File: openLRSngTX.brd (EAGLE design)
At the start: 50 x 40 mm, 33 parts, among them IC1 RFM23BPSMD, J1 AVR_SPI_PRG_6PTH, Q1 MMBT2222, U1 ATMEGA328P, X1 BU-SMA-V, Y1 16MHz

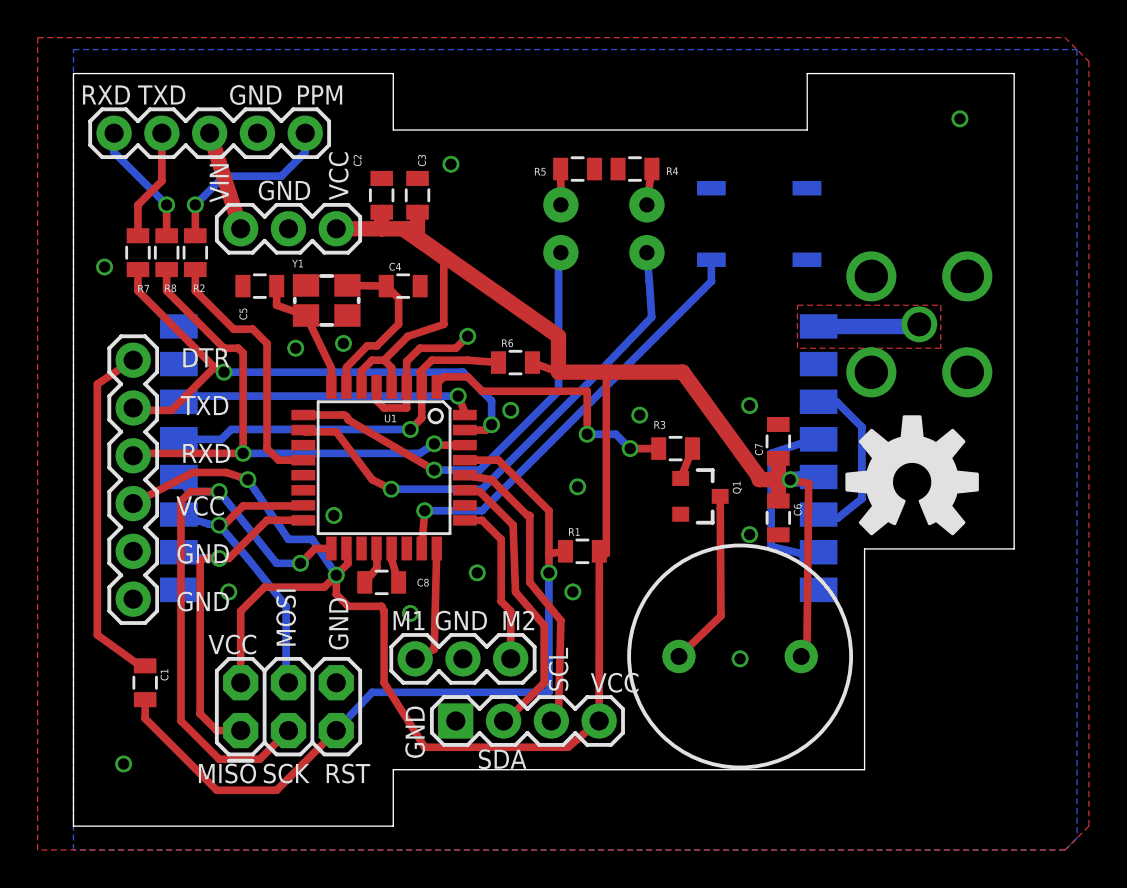
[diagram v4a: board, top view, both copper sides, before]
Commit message: Add possibility for wired boind button.
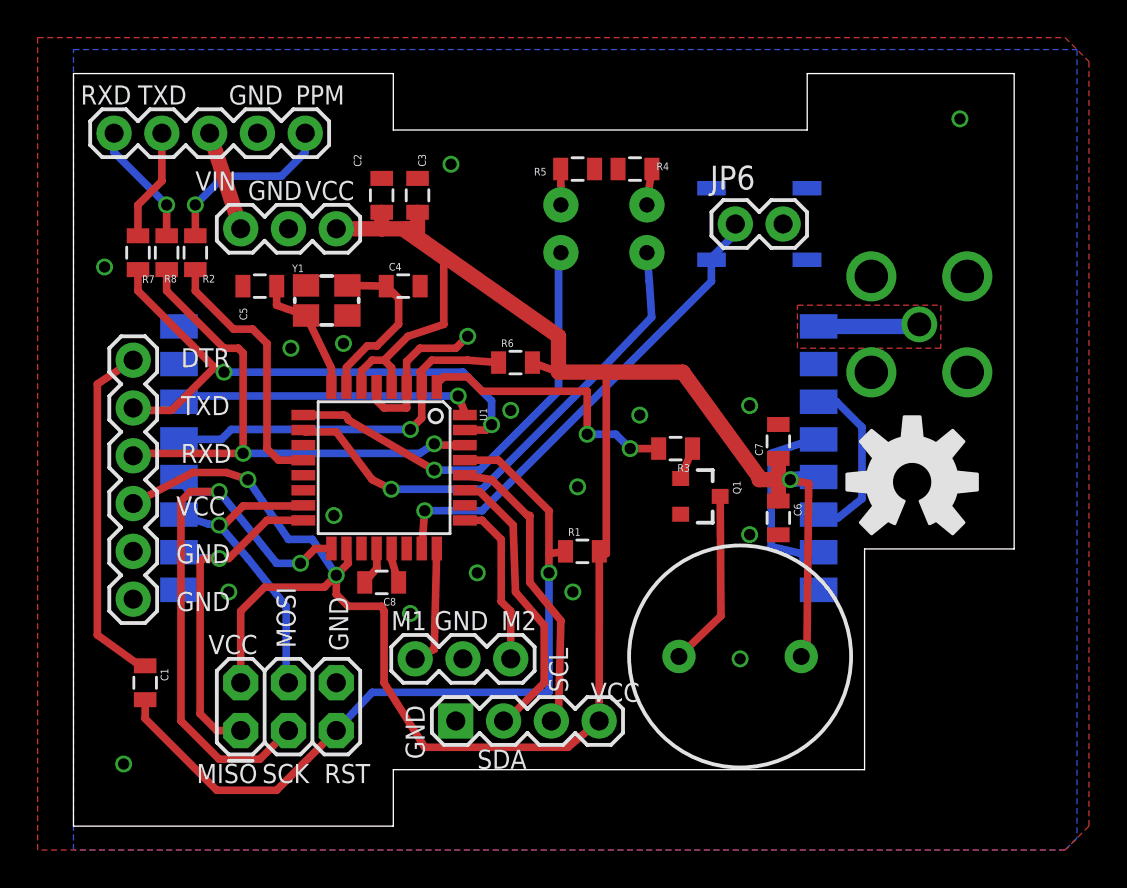
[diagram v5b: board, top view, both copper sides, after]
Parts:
- added JP6: (no value), SparkFun-Connectors:1X02
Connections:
- net GND: now also JP6.2
- net N$15: now also JP6.1
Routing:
- net N$15: track 23.4 -> 25.9 mm
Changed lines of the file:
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@@
 <layer number="27" name="tValues" color="7" fill="1" visible="yes" active="yes"/>
 <layer number="28" name="bValues" color="7" fill="1" visible="yes" active="yes"/>
-<layer number="29" name="tStop" color="7" fill="3" visible="yes" active="yes"/>
+<layer number="29" name="tStop" color="7" fill="3" visible="no" active="yes"/>
 <layer number="30" name="bStop" color="7" fill="6" visible="no" active="yes"/>
 <layer number="31" name="tCream" color="7" fill="4" visible="no" active="yes"/>
@@
 <text x="11.176" y="38.354" size="1.016" layer="25">PPM</text>
 <text x="7.62" y="38.354" size="1.016" layer="25">GND</text>
-<text x="6.604" y="35.306" size="1.016" layer="25" rot="R270">VIN</text>
+<text x="5.842" y="33.782" size="1.016" layer="25">VIN</text>
 <text x="2.794" y="38.354" size="1.016" layer="25">TXD</text>
-<text x="13.97" y="33.274" size="1.016" layer="25" rot="R90">VCC</text>
-<text x="9.144" y="33.274" size="1.016" layer="25">GND</text>
+<text x="11.684" y="33.274" size="1.016" layer="25">VCC</text>
+<text x="8.636" y="33.274" size="1.016" layer="25">GND</text>
 <text x="18.034" y="3.556" size="1.016" layer="25" rot="R90">GND</text>
 <text x="20.828" y="3.048" size="1.016" layer="25">SDA</text>
 <text x="25.654" y="7.112" size="1.016" layer="25" rot="R90">SCL</text>
-<text x="29.464" y="8.128" size="1.016" layer="25" rot="R180">VCC</text>
+<text x="29.464" y="7.62" size="1.016" layer="25" rot="R180">VCC</text>
 <text x="9.144" y="10.16" size="1.016" layer="25" rot="R180">VCC</text>
 <text x="9.144" y="3.302" size="1.016" layer="25" rot="R180">MISO</text>
@@
 </autorouter>
 <elements>
-<element name="U1" library="SparkFun-DigitalIC" package="TQFP32-08" value="ATMEGA328P" x="15.875" y="19.05" smashed="yes" rot="R270">
+<element name="U1" library="SparkFun-DigitalIC" package="TQFP32-08" value="ATMEGA328P" x="15.875" y="19.05" rot="R270">
 <attribute name="PROD_ID" value="IC-09069" x="-8.255" y="1.27" size="1.778" layer="27" rot="R270" display="off"/>
-<attribute name="NAME" x="15.875" y="21.463" size="0.4064" layer="25"/>
-<attribute name="VALUE" x="9.525" y="21.59" size="0.4064" layer="27" rot="R270"/>
 </element>
 <element name="C1" library="SparkFun-Capacitors" package="0805" value="100n" x="3.175" y="7.62" rot="R270"/>
@@
 <element name="R1" library="SparkFun-Resistors" package="0805" value="10k" x="26.416" y="14.605"/>
 <element name="R2" library="SparkFun-Resistors" package="0805" value="1k" x="5.842" y="30.48" smashed="yes" rot="R270">
-<attribute name="NAME" x="5.715" y="28.3845" size="0.4064" layer="25"/>
-<attribute name="VALUE" x="5.7785" y="27.813" size="0.4064" layer="27"/>
-</element>
-<element name="R3" library="SparkFun-Resistors" package="0805" value="1k" x="31.369" y="20.066" smashed="yes" rot="R180">
-<attribute name="NAME" x="30.861" y="21.5265" size="0.4064" layer="25" rot="R180"/>
-<attribute name="VALUE" x="31.877" y="21.463" size="0.4064" layer="27" rot="R180"/>
-</element>
+<attribute name="NAME" x="6.223" y="28.8925" size="0.4064" layer="25"/>
+<attribute name="VALUE" x="6.2865" y="28.321" size="0.4064" layer="27"/>
+</element>
+<element name="R3" library="SparkFun-Resistors" package="0805" value="1k" x="31.369" y="20.066" rot="R180"/>
 <element name="R4" library="SparkFun-Resistors" package="0805" value="220R" x="29.21" y="34.925" smashed="yes">
-<attribute name="NAME" x="30.861" y="34.6075" size="0.4064" layer="25"/>
-<attribute name="VALUE" x="28.6385" y="35.814" size="0.4064" layer="27"/>
+<attribute name="NAME" x="30.353" y="34.8615" size="0.4064" layer="25"/>
+<attribute name="VALUE" x="28.6385" y="35.56" size="0.4064" layer="27"/>
 </element>
 <element name="R5" library="SparkFun-Resistors" package="0805" value="220R" x="26.162" y="34.925" smashed="yes" rot="R180">
 <attribute name="NAME" x="24.511" y="34.9885" size="0.4064" layer="25" rot="R180"/>
-<attribute name="VALUE" x="26.4795" y="36.322" size="0.4064" layer="27" rot="R180"/>
+<attribute name="VALUE" x="26.4795" y="36.068" size="0.4064" layer="27" rot="R180"/>
 </element>
 <element name="LED1" library="SparkFun-LED" package="LED3MM" value="RED" x="29.845" y="31.75" smashed="yes" rot="MR90"/>
@@
 <attribute name="OC_FARNELL" value="unknown" x="44.323" y="26.67" size="1.778" layer="28" rot="MR0" display="off"/>
 </element>
-<element name="Y1" library="crystal_3225" package="CRYSTAL-SMD-5X3" value="16MHz" x="12.827" y="27.94" smashed="yes">
-<attribute name="NAME" x="10.987" y="29.699" size="0.4064" layer="25"/>
-<attribute name="VALUE" x="10.987" y="25.846" size="0.4064" layer="27"/>
-</element>
+<element name="Y1" library="crystal_3225" package="CRYSTAL-SMD-5X3" value="16MHz" x="12.827" y="27.94"/>
 <element name="JP1" library="SparkFun-Connectors" package="1X05" value="IN" x="11.684" y="36.83" smashed="yes" rot="R180"/>
 <element name="JP4" library="SparkFun-Connectors" package="1X03" value="REG" x="8.255" y="31.75" smashed="yes"/>
@@
 <element name="C7" library="SparkFun-Capacitors" package="0805" value="100n" x="36.83" y="20.447" rot="R90"/>
 <element name="R6" library="SparkFun-Resistors" package="0805" value="1k" x="22.86" y="24.638"/>
-<element name="C8" library="SparkFun-Capacitors" package="0805" value="100n" x="15.748" y="12.954" smashed="yes" rot="R180">
-<attribute name="NAME" x="18.288" y="13.1445" size="0.4064" layer="25" rot="R180"/>
-<attribute name="VALUE" x="18.796" y="13.843" size="0.4064" layer="27" rot="R180"/>
-</element>
+<element name="C8" library="SparkFun-Capacitors" package="0805" value="100n" x="15.748" y="12.954" rot="R180"/>
 <element name="S1" library="SparkFun-Electromechanical" package="TACTILE_SWITCH_SMD" value="SWITCH-MOMENTARY-2SMD" x="35.814" y="32.004" smashed="yes" rot="MR180">
 <attribute name="VALUE" x="34.925" y="34.036" size="0.4064" layer="28" rot="MR180"/>
 </element>
 <element name="R7" library="SparkFun-Resistors" package="0805" value="1k" x="2.794" y="30.48" smashed="yes" rot="R270">
-<attribute name="NAME" x="3.429" y="28.7655" size="0.4064" layer="25" rot="R180"/>
-<attribute name="VALUE" x="2.7305" y="27.813" size="0.4064" layer="27"/>
+<attribute name="NAME" x="3.683" y="29.2735" size="0.4064" layer="25" rot="R180"/>
+<attribute name="VALUE" x="2.9845" y="28.321" size="0.4064" layer="27"/>
 </element>
 <element name="U$1" library="SparkFun-Aesthetics" package="OSHW-LOGO-L" value="" x="43.942" y="18.288" rot="MR0"/>
@@
 <element name="U$2" library="SparkFun-Aesthetics" package="OSHW-LOGO-L" value="" x="43.942" y="18.288"/>
 <element name="R8" library="SparkFun-Resistors" package="0805" value="1k" x="4.318" y="30.48" smashed="yes" rot="R270">
-<attribute name="NAME" x="4.191" y="28.3845" size="0.4064" layer="25"/>
-<attribute name="VALUE" x="4.2545" y="27.813" size="0.4064" layer="27"/>
-</element>
+<attribute name="NAME" x="4.191" y="28.8925" size="0.4064" layer="25"/>
+<attribute name="VALUE" x="4.2545" y="28.321" size="0.4064" layer="27"/>
+</element>
+<element name="JP6" library="SparkFun-Connectors" package="1X02" value="" x="34.544" y="32.004"/>
 </elements>
 <signals>
@@
 <contactref element="Y1" pad="2"/>
 <via x="13.716" y="25.654" extent="1-16" drill="0.6"/>
-<via x="11.176" y="25.4" extent="1-16" drill="0.6"/>
+<via x="10.922" y="25.4" extent="1-16" drill="0.6"/>
 <via x="13.208" y="16.51" extent="1-16" drill="0.6"/>
+<contactref element="JP6" pad="2"/>
 </signal>
 <signal name="VCC">
@@
 <wire x1="33.274" y1="28.956" x2="33.274" y2="30.099" width="0.4064" layer="16"/>
 <wire x1="18.034" y1="16.764" x2="17.875" y2="14.7574" width="0.4064" layer="1"/>
+<contactref element="JP6" pad="1"/>
+<wire x1="33.274" y1="30.099" x2="33.274" y2="30.226" width="0.4064" layer="16"/>
+<wire x1="33.274" y1="30.226" x2="34.544" y2="31.496" width="0.4064" layer="16"/>
+<wire x1="34.544" y1="31.496" x2="34.544" y2="32.004" width="0.4064" layer="16"/>
 </signal>
 <signal name="N$16">

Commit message: Add mountting holes.
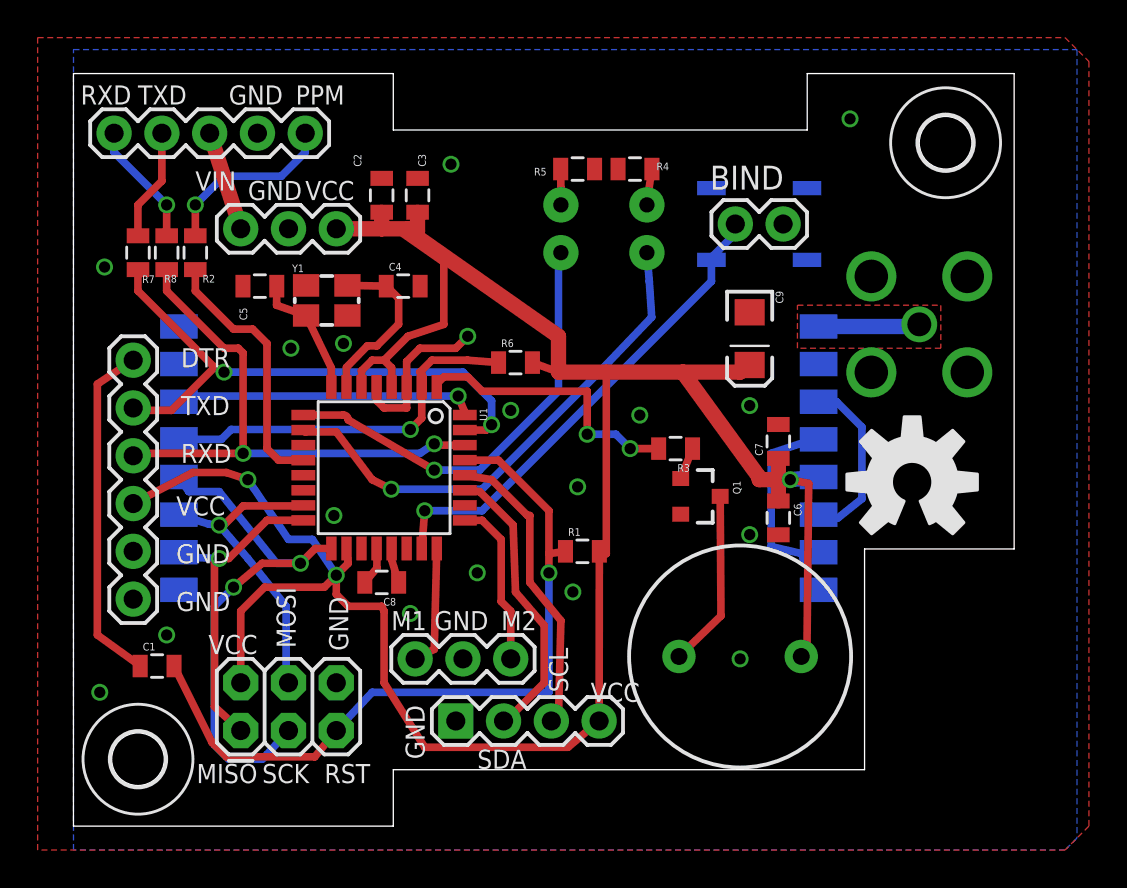
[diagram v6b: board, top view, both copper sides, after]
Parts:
- added C9: 10uF, SparkFun-Capacitors:EIA3216
- added U$3, U$4: (no value), holes:2,8
- S1: value SWITCH-MOMENTARY-2SMD -> BIND
- moved C1 1.09 mm to (3.81, 8.51), turned to 0 degrees
- renumbered JP6 to BIND
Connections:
- net GND: now also C9.C
- net VCC: now also C9.A
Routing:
- net VCC: track 129.4 -> 133.1 mm
- net SCK: track 31.8 -> 28.4 mm
- net /RESET: track 42.4 -> 40.4 mm
- net MISO: track 19.3 -> 17.5 mm
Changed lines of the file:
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@@
 <attribute name="PROD_ID" value="IC-09069" x="-8.255" y="1.27" size="1.778" layer="27" rot="R270" display="off"/>
 </element>
-<element name="C1" library="SparkFun-Capacitors" package="0805" value="100n" x="3.175" y="7.62" rot="R270"/>
+<element name="C1" library="SparkFun-Capacitors" package="0805" value="100n" x="3.81" y="8.509"/>
 <element name="C2" library="SparkFun-Capacitors" package="0805" value="100n" x="15.748" y="33.528" smashed="yes" rot="R90">
 <attribute name="NAME" x="14.6685" y="35.052" size="0.4064" layer="25" rot="R90"/>
@@
 <element name="R6" library="SparkFun-Resistors" package="0805" value="1k" x="22.86" y="24.638"/>
 <element name="C8" library="SparkFun-Capacitors" package="0805" value="100n" x="15.748" y="12.954" rot="R180"/>
-<element name="S1" library="SparkFun-Electromechanical" package="TACTILE_SWITCH_SMD" value="SWITCH-MOMENTARY-2SMD" x="35.814" y="32.004" smashed="yes" rot="MR180">
+<element name="S1" library="SparkFun-Electromechanical" package="TACTILE_SWITCH_SMD" value="BIND" x="35.814" y="32.004" smashed="yes" rot="MR180">
 <attribute name="VALUE" x="34.925" y="34.036" size="0.4064" layer="28" rot="MR180"/>
 </element>
@@
 <attribute name="VALUE" x="4.2545" y="28.321" size="0.4064" layer="27"/>
 </element>
-<element name="JP6" library="SparkFun-Connectors" package="1X02" value="" x="34.544" y="32.004"/>
+<element name="BIND" library="SparkFun-Connectors" package="1X02" value="" x="34.544" y="32.004"/>
+<element name="U$3" library="holes" package="2,8" value="" x="2.794" y="3.556"/>
+<element name="U$4" library="holes" package="2,8" value="" x="45.72" y="36.322"/>
+<element name="C9" library="SparkFun-Capacitors" package="EIA3216" value="10uF" x="35.306" y="25.908" rot="R270">
+<attribute name="PROD_ID" value="CAP-00811" x="35.306" y="25.908" size="1.778" layer="27" rot="R270" display="off"/>
+</element>
 </elements>
 <signals>
@@
 <contactref element="S1" pad="3"/>
 <via x="35.306" y="15.494" extent="1-16" drill="0.6"/>
-<via x="7.62" y="12.446" extent="1-16" drill="0.6"/>
+<via x="4.318" y="10.16" extent="1-16" drill="0.6"/>
 <via x="25.908" y="12.446" extent="1-16" drill="0.6"/>
 <via x="26.162" y="18.034" extent="1-16" drill="0.6"/>
@@
 <via x="29.464" y="21.844" extent="1-16" drill="0.6"/>
 <via x="20.828" y="13.462" extent="1-16" drill="0.6"/>
-<via x="2.032" y="3.302" extent="1-16" drill="0.6"/>
-<via x="46.482" y="37.592" extent="1-16" drill="0.6"/>
+<via x="0.762" y="7.112" extent="1-16" drill="0.6"/>
+<via x="40.64" y="37.592" extent="1-16" drill="0.6"/>
 <contactref element="JP5" pad="2"/>
 <wire x1="16.275" y1="14.7574" x2="16.256" y2="14.224" width="0.4064" layer="1"/>
@@
 <via x="10.922" y="25.4" extent="1-16" drill="0.6"/>
 <via x="13.208" y="16.51" extent="1-16" drill="0.6"/>
-<contactref element="JP6" pad="2"/>
+<contactref element="BIND" pad="2"/>
+<contactref element="C9" pad="C"/>
 </signal>
 <signal name="VCC">
@@
 <wire x1="38.443603125" y1="18.21205" x2="37.465" y2="18.415" width="0.4064" layer="1"/>
 <wire x1="27.686" y1="14.478" x2="27.316" y2="14.605" width="0.4064" layer="1"/>
+<contactref element="C9" pad="A"/>
+<wire x1="31.75" y1="24.13" x2="34.798" y2="24.13" width="0.8128" layer="1"/>
+<wire x1="34.798" y1="24.13" x2="35.306" y2="24.508" width="0.8128" layer="1"/>
 </signal>
 <signal name="RXD">
@@
 <wire x1="0.635" y1="23.495" x2="0.635" y2="10.16" width="0.4064" layer="1"/>
 <wire x1="0.635" y1="10.16" x2="2.91" y2="8.52" width="0.4064" layer="1"/>
-<wire x1="2.91" y1="8.52" x2="3.175" y2="8.52" width="0.4064" layer="1"/>
+<wire x1="2.91" y1="8.52" x2="2.91" y2="8.509" width="0.4064" layer="1"/>
 </signal>
 <signal name="/RESET">
@@
 <contactref element="U1" pad="29"/>
 <contactref element="J1" pad="5"/>
-<wire x1="3.175" y1="6.72" x2="3.175" y2="5.715" width="0.4064" layer="1"/>
-<wire x1="3.175" y1="5.715" x2="6.985" y2="1.905" width="0.4064" layer="1"/>
-<wire x1="6.985" y1="1.905" x2="10.16" y2="1.905" width="0.4064" layer="1"/>
-<wire x1="10.16" y1="1.905" x2="13.335" y2="5.08" width="0.4064" layer="1"/>
+<wire x1="4.71" y1="8.509" x2="6.731" y2="4.445" width="0.4064" layer="1"/>
+<wire x1="6.731" y1="4.445" x2="7.493" y2="3.683" width="0.4064" layer="1"/>
+<wire x1="7.493" y1="3.683" x2="12.192" y2="3.683" width="0.4064" layer="1"/>
+<wire x1="12.192" y1="3.683" x2="13.335" y2="5.08" width="0.4064" layer="1"/>
 <wire x1="20.1676" y1="19.45" x2="21.952" y2="19.45" width="0.4064" layer="1"/>
 <wire x1="21.952" y1="19.45" x2="24.638" y2="16.764" width="0.4064" layer="1"/>
@@
 <contactref element="U1" pad="16"/>
 <contactref element="IC1" pad="10"/>
-<wire x1="8.255" y1="5.08" x2="6.985" y2="5.08" width="0.4064" layer="1"/>
-<wire x1="6.985" y1="5.08" x2="6.096" y2="5.969" width="0.4064" layer="1"/>
 <wire x1="11.5824" y1="16.25" x2="11.5764" y2="16.256" width="0.4064" layer="1"/>
 <wire x1="11.5764" y1="16.256" x2="9.652" y2="16.256" width="0.4064" layer="1"/>
@@
 <wire x1="7.112" y1="14.224" x2="5.16" y2="14.304" width="0.4064" layer="16"/>
 <wire x1="5.16" y1="14.304" x2="4.971" y2="14.558" width="0.4064" layer="16"/>
-<wire x1="6.096" y1="5.969" x2="6.096" y2="14.05" width="0.4064" layer="1"/>
-<wire x1="6.096" y1="14.05" x2="6.27" y2="14.224" width="0.4064" layer="1"/>
-<wire x1="6.27" y1="14.224" x2="7.112" y2="14.224" width="0.4064" layer="1"/>
+<wire x1="6.858" y1="6.35" x2="6.858" y2="14.05" width="0.4064" layer="1"/>
+<wire x1="8.255" y1="5.08" x2="6.858" y2="6.35" width="0.4064" layer="1"/>
+<wire x1="6.858" y1="14.05" x2="7.112" y2="14.224" width="0.4064" layer="1"/>
 </signal>
 <signal name="SCK">
@@
 <contactref element="U1" pad="17"/>
 <contactref element="IC1" pad="12"/>
-<wire x1="10.795" y1="5.08" x2="9.271" y2="3.556" width="0.4064" layer="1"/>
-<wire x1="9.271" y1="3.556" x2="7.112" y2="3.556" width="0.4064" layer="1"/>
-<wire x1="7.112" y1="3.556" x2="5.08" y2="5.588" width="0.4064" layer="1"/>
-<wire x1="5.08" y1="5.588" x2="5.08" y2="17.272" width="0.4064" layer="1"/>
-<wire x1="5.08" y1="17.272" x2="5.588" y2="17.78" width="0.4064" layer="1"/>
-<wire x1="5.588" y1="17.78" x2="7.112" y2="17.78" width="0.4064" layer="1"/>
-<via x="7.112" y="17.78" extent="1-16" drill="0.6"/>
 <wire x1="7.112" y1="17.78" x2="10.16" y2="13.97" width="0.4064" layer="16"/>
 <wire x1="10.16" y1="13.97" x2="11.43" y2="13.97" width="0.4064" layer="16"/>
@@
 <wire x1="4.971" y1="18.558" x2="5.495" y2="17.78" width="0.4064" layer="16"/>
 <wire x1="5.495" y1="17.78" x2="7.112" y2="17.78" width="0.4064" layer="16"/>
+<wire x1="10.795" y1="5.08" x2="9.652" y2="3.81" width="0.4064" layer="16"/>
+<wire x1="9.652" y1="3.81" x2="9.398" y2="3.556" width="0.4064" layer="16"/>
+<wire x1="9.398" y1="3.556" x2="7.62" y2="3.556" width="0.4064" layer="16"/>
+<wire x1="7.62" y1="3.556" x2="6.858" y2="4.318" width="0.4064" layer="16"/>
+<wire x1="6.858" y1="4.318" x2="6.858" y2="11.684" width="0.4064" layer="16"/>
+<wire x1="6.858" y1="11.684" x2="7.874" y2="12.7" width="0.4064" layer="16"/>
+<via x="7.874" y="12.7" extent="1-16" drill="0.6"/>
+<wire x1="7.874" y1="12.7" x2="9.398" y2="13.97" width="0.4064" layer="1"/>
+<wire x1="9.398" y1="13.97" x2="11.43" y2="13.97" width="0.4064" layer="1"/>
 </signal>
 <signal name="N$1">
@@
 <wire x1="33.274" y1="28.956" x2="33.274" y2="30.099" width="0.4064" layer="16"/>
 <wire x1="18.034" y1="16.764" x2="17.875" y2="14.7574" width="0.4064" layer="1"/>
-<contactref element="JP6" pad="1"/>
+<contactref element="BIND" pad="1"/>
 <wire x1="33.274" y1="30.099" x2="33.274" y2="30.226" width="0.4064" layer="16"/>
 <wire x1="33.274" y1="30.226" x2="34.544" y2="31.496" width="0.4064" layer="16"/>
